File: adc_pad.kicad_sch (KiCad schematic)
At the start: 20 parts, among them SW10 TS-1187, SW11 TS-1187, SW4 TS-1187, SW5 TS-1187, SW6 TS-1187, SW7 TS-1187, SW8 TS-1187, SW9 TS-1187

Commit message: Rev.2 (260322)
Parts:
- C28, C29: footprint Harucom_Board:C_0402_1005Metric_Pad0.47x0.53mm -> Capacitor_SMD:C_0603_1608Metric; LCSC (none) -> C14663
- R34, R35, R39, R40: footprint Resistor_SMD:R_0402_1005Metric -> Resistor_SMD:R_0603_1608Metric; LCSC (none) -> C21190
- R36, R41: footprint Resistor_SMD:R_0402_1005Metric -> Resistor_SMD:R_0603_1608Metric; LCSC (none) -> C4190
- R37, R42: footprint Resistor_SMD:R_0402_1005Metric -> Resistor_SMD:R_0603_1608Metric; LCSC (none) -> C23162
- R38, R43: footprint Resistor_SMD:R_0402_1005Metric -> Resistor_SMD:R_0603_1608Metric; LCSC (none) -> C25804
- SW10: renamed from SW8; value TS-1187 -> TS6612TP; footprint Button_Switch_SMD:SW_Push_1P1T_XKB_TS-1187A -> Harucom_Board:KEY-SMD_4P-L6.0-W6.0-P4.50-LS9.0; LCSC (none) -> C5369159
- SW11: renamed from SW9; value TS-1187 -> TS6612TP; footprint Button_Switch_SMD:SW_Push_1P1T_XKB_TS-1187A -> Harucom_Board:KEY-SMD_4P-L6.0-W6.0-P4.50-LS9.0; LCSC (none) -> C5369159
- SW4, SW5, SW6, SW7: value TS-1187 -> TS6612TP; footprint Button_Switch_SMD:SW_Push_1P1T_XKB_TS-1187A -> Harucom_Board:KEY-SMD_4P-L6.0-W6.0-P4.50-LS9.0; LCSC (none) -> C5369159
- SW8: renamed from SW10; value TS-1187 -> TS6612TP; footprint Button_Switch_SMD:SW_Push_1P1T_XKB_TS-1187A -> Harucom_Board:KEY-SMD_4P-L6.0-W6.0-P4.50-LS9.0; LCSC (none) -> C5369159
- SW9: renamed from SW11; value TS-1187 -> TS6612TP; footprint Button_Switch_SMD:SW_Push_1P1T_XKB_TS-1187A -> Harucom_Board:KEY-SMD_4P-L6.0-W6.0-P4.50-LS9.0; LCSC (none) -> C5369159
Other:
- moved on the sheet: SW10, SW11

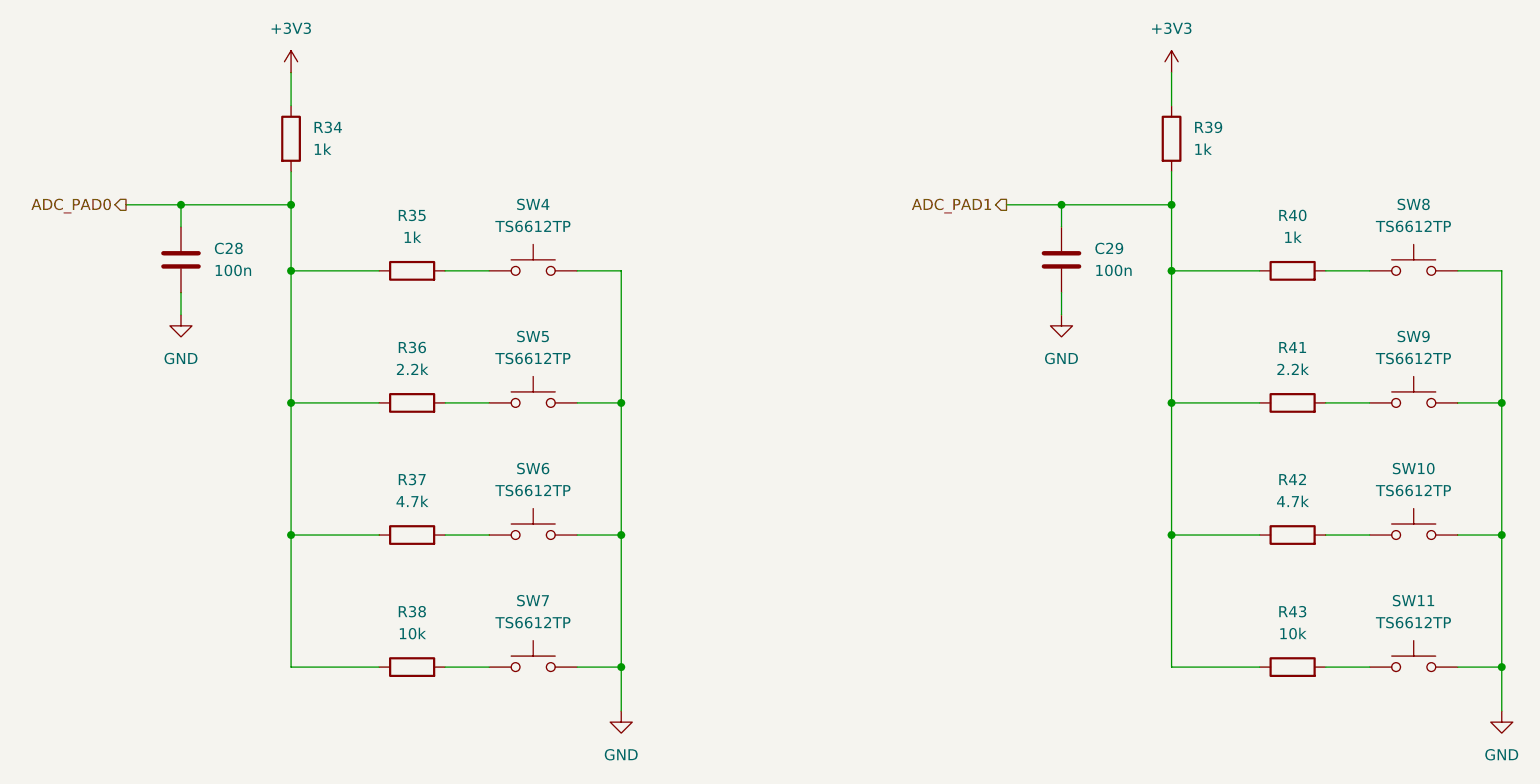
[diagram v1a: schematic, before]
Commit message: Rev. 2B: Change PSRAM package from SOP-8 to USON-8L.
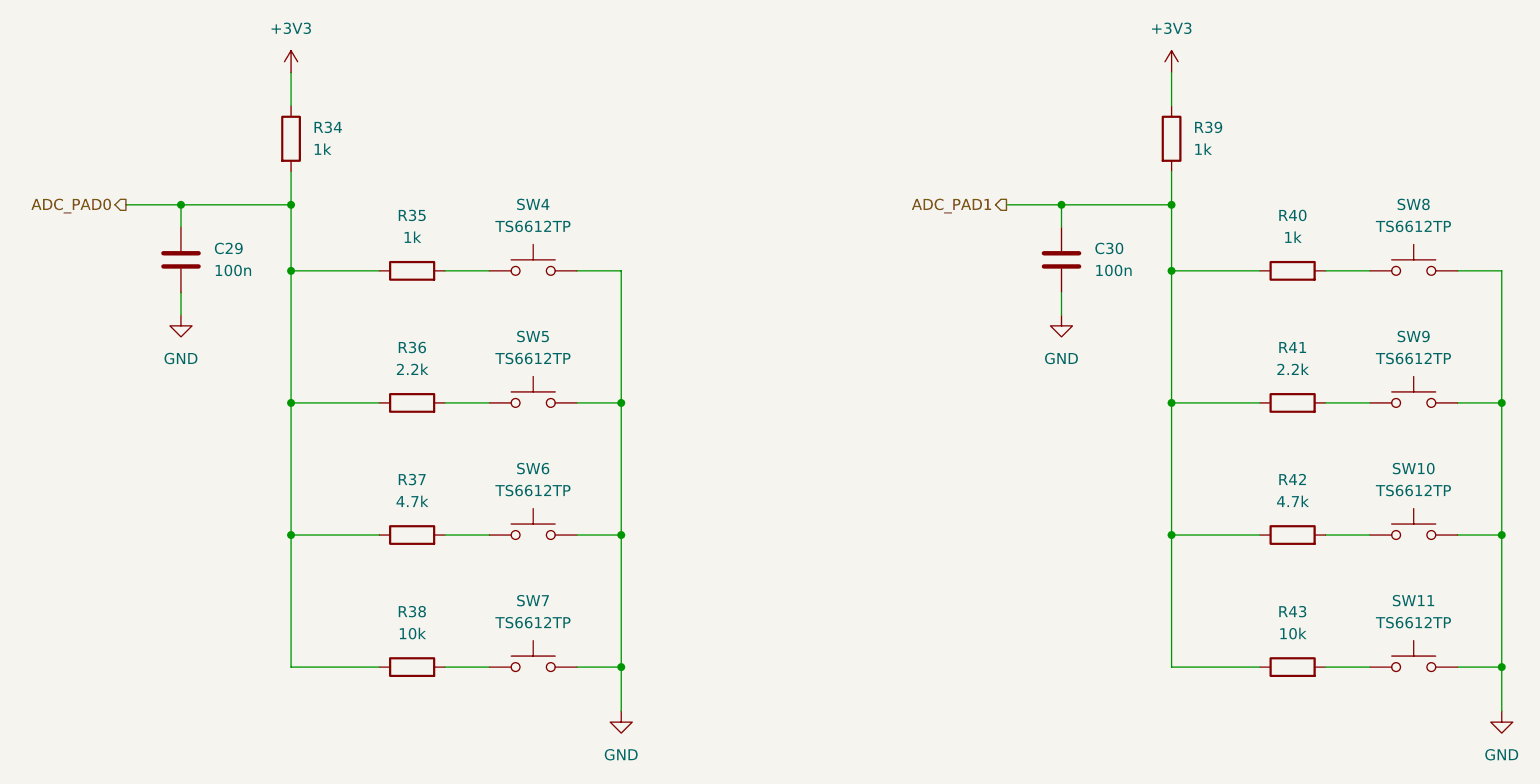
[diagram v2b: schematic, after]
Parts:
- renumbered C28 to C29, C29 to C30
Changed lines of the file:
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@@
 	(title_block
 		(title "Harucom-board")
-		(date "2026-03-22")
-		(rev "2")
+		(date "2026-03-23")
+		(rev "2B")
 		(comment 1 "https://github.com/harukasan/harucom-board/")
 		(comment 2 "SPDX-License-Identifier: CERN-OHL-P-2.0")
@@
 		(dnp no)
 		(fields_autoplaced yes)
-		(property "Reference" "C28"
+		(property "Reference" "C29"
 			(at 54.61 73.6599 0)
 			(effects
@@
 			(project ""
 				(path "/0cb5192e-ac62-478f-bacb-beb1b9be1a5b/9eade9ea-9a30-4a42-95b8-9774a26a3a8f"
-					(reference "C28")
+					(reference "C29")
 					(unit 1)
 				)
@@
 		(dnp no)
 		(fields_autoplaced yes)
-		(property "Reference" "C29"
+		(property "Reference" "C30"
 			(at 156.21 73.6599 0)
 			(effects
@@
 			(project ""
 				(path "/0cb5192e-ac62-478f-bacb-beb1b9be1a5b/9eade9ea-9a30-4a42-95b8-9774a26a3a8f"
-					(reference "C29")
+					(reference "C30")
 					(unit 1)
 				)
